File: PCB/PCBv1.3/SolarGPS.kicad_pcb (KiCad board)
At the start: 2 copper layers, 75 x 27 mm, 58 parts, among them J1 Conn_01x10_Female, J2 Solar1+, J3 GND, J4 Conn_02x03_Odd_Even, J5 Solar2+, J6 GND, J7 Screw_Terminal_01x01, J8 Conn_01x04_Male, U1 STM32L011G3Ux, U2 MAX-M10Q, U5 BQ25505, U6 LIS3DH, U7 TPS63802, Y1 32.768

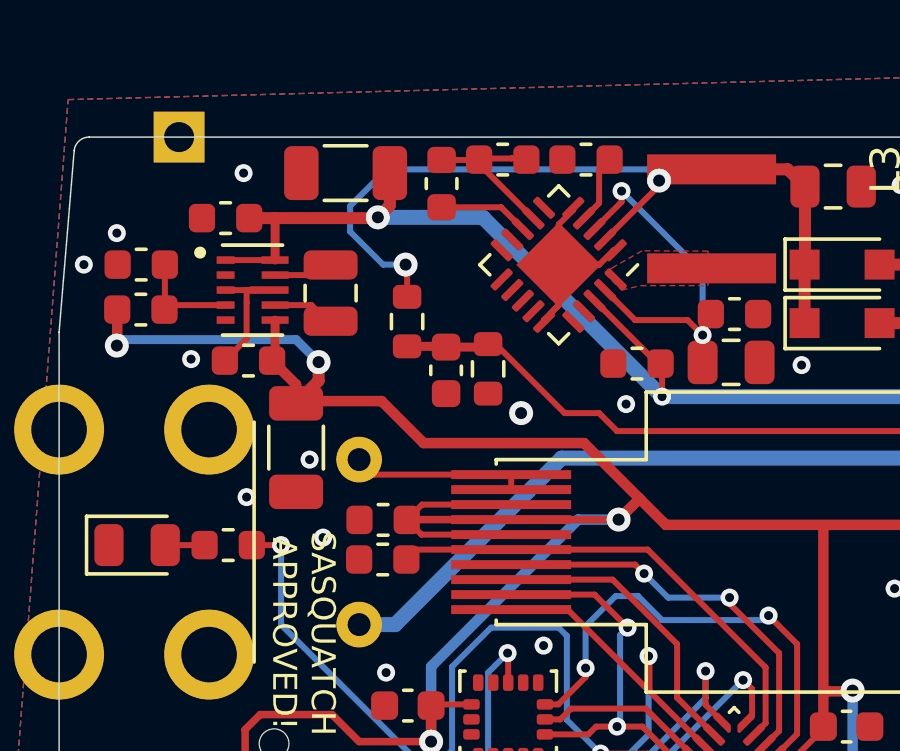
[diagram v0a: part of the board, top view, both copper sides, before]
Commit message: Move symbols to lib
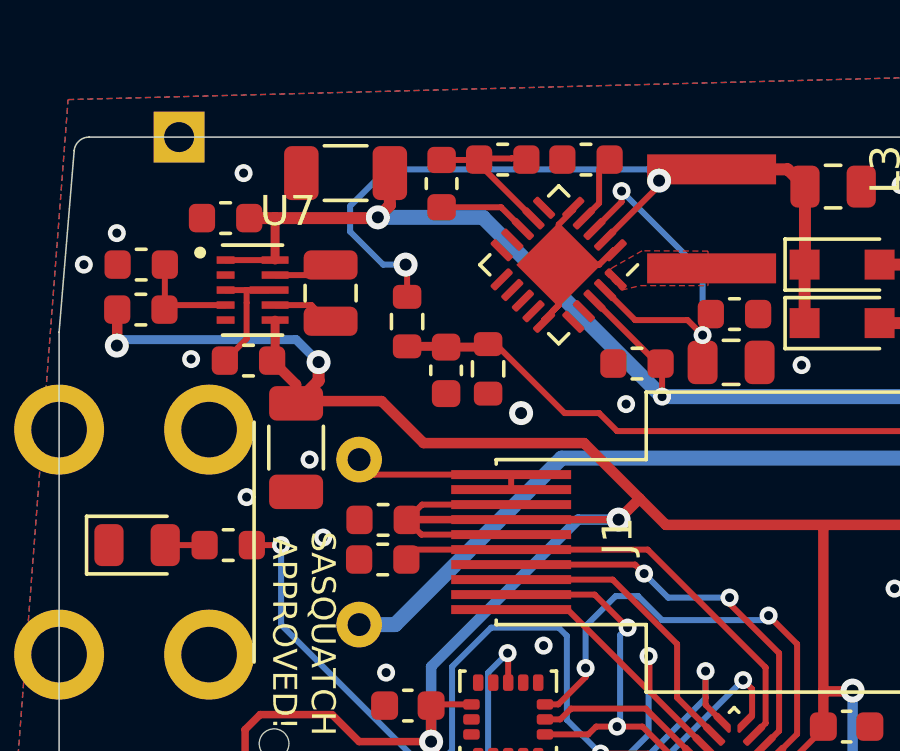
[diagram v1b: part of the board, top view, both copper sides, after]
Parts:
- C14: footprint Veridian-Library-KiCad:SCCT20E106SRB -> Heliograph:SCCT20E106SRB
- J1: footprint Margo_Lib:LS013B7DH03 -> Heliograph:LS013B7DH03
- L3: footprint Margo_Lib:744031220 -> Heliograph:744031220
- U7: footprint Margo_Lib:VREG_TPS63802DLAR -> Heliograph:VREG_TPS63802DLAR

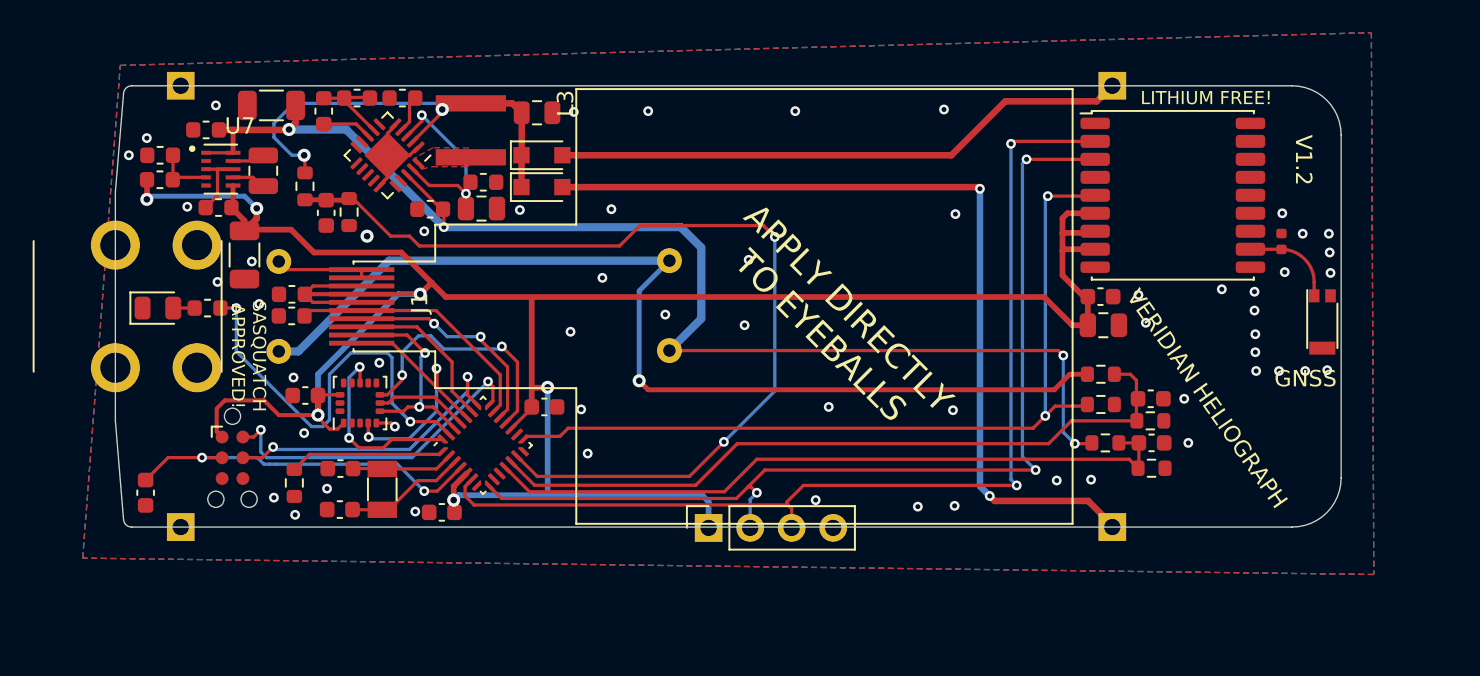
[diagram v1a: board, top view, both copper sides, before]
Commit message: Drop MPPT buck for diode cost
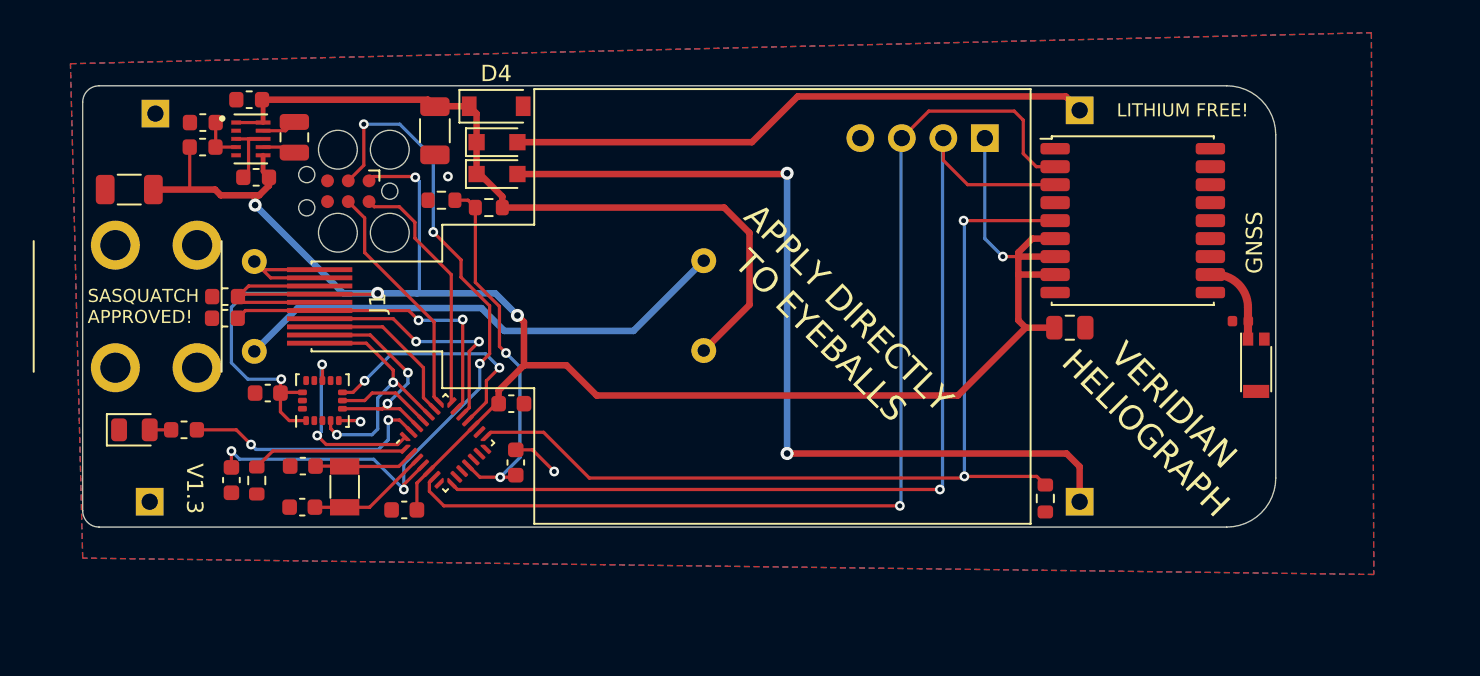
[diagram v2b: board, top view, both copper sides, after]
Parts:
- removed C15, C16, C19, C28, C6: 10nF, Capacitor_SMD:C_0603_1608Metric
- removed C2, C3: 4.7uF, Capacitor_SMD:C_0805_2012Metric
- removed C21: 1uF, Capacitor_SMD:C_0603_1608Metric
- removed L3: 22uH, Heliograph:744031220
- removed R14, R15, R2, R6: 1M, Resistor_SMD:R_0603_1608Metric
- removed ROV3: 4.30M, Resistor_SMD:R_0603_1608Metric
- removed ROV4: 8.66M, Resistor_SMD:R_0603_1608Metric
- removed U5: BQ25505, Package_DFN_QFN:QFN-20-1EP_3.5x3.5mm_P0.5mm_EP2x2mm
- added D4: 6V, Diode_SMD:D_SOD-123, F.Cu at (72.3, 51.2)
- J4: footprint Connector:Tag-Connect_TC2030-IDC-NL_2x03_P1.27mm_Vertical -> Connector:Tag-Connect_TC2030-IDC-FP_2x03_P1.27mm_Vertical
- J8: moved to B.Cu
- moved R13 46.4 mm to (69.0, 57.0), turned to 0 degrees
- moved R12 40.4 mm to (71.8, 57.5), turned to 0 degrees
- moved C23 38.9 mm to (73.5, 73.0), turned to -90 degrees
- moved J8 29.2 mm to (102.2, 53.2)
- moved J4 17.8 mm to (63.2, 56.5), turned to 180 degrees
- moved C12 10.1 mm to (68.5, 52.8), turned to 90 degrees
- moved C7 8.11 mm to (49.9, 56.4), turned to 0 degrees
- moved D2 7.59 mm to (50.2, 71.0)
- moved R3 7.59 mm to (53.2, 71.0)
- moved R7 6.68 mm to (105.9, 75.2), turned to 90 degrees
- moved C1 5.49 mm to (117.8, 64.4), turned to 0 degrees
- moved C18 5.31 mm to (56.1, 74.1)
- moved AE1 4.84 mm to (118.8, 67.1)
- moved C20 4.09 mm to (55.7, 64.2)
- moved C9 4.09 mm to (55.7, 62.9)
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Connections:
- D1 pad 1: SOLAR+ -> VBAT
- D3 pad 1: SOLAR+ -> VBAT
- U1 pad 12: VBATMID_SENSE -> unconnected-(U1-Pad12)
- U1 pad 13: SOLAR_SENSE1 -> unconnected-(U1-Pad13)
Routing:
- net SOLAR_SENSE1: track 58.7 -> 0.00 mm, vias 2 -> 0
- net VBATMID_SENSE: track 44.5 -> 0.00 mm
- net VBAT: track 79.5 -> 47.2 mm, vias 4 -> 0
- net VBATMID: track 62.4 -> 31.0 mm, vias 1 -> 0
- net SOLAR+: track 27.6 -> 0.00 mm, vias 2 -> 0
- net RESET: track 22.5 -> 47.4 mm, vias 2 -> 5
- net VBAT_SENSE: track 43.2 -> 22.8 mm, vias 0 -> 2
- net VSTOR: track 13.2 -> 0.00 mm, vias 2 -> 0
- net LED: track 25.8 -> 15.4 mm
- net VDD: track 156.3 -> 150.4 mm
- net Net-(ROV3-Pad1): track 5.22 -> 0.00 mm
- net GPS_EXINT: track 52.0 -> 57.0 mm
- net /SWDIO: track 20.3 -> 15.3 mm, vias 2 -> 0
- net /SWDCLK: track 18.4 -> 14.6 mm, vias 2 -> 0
- net DISP_EN: track 16.1 -> 19.9 mm, vias 0 -> 2
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- removed copper zone on F.Cu, net Net-(L3-Pad2)
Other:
- board size 75 x 27 mm -> 73 x 27 mm
- board text added: "V1.3"
- board text added: "VDD MOSI MISO GND"
- board text removed: "V1.2"

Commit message: Change LCD
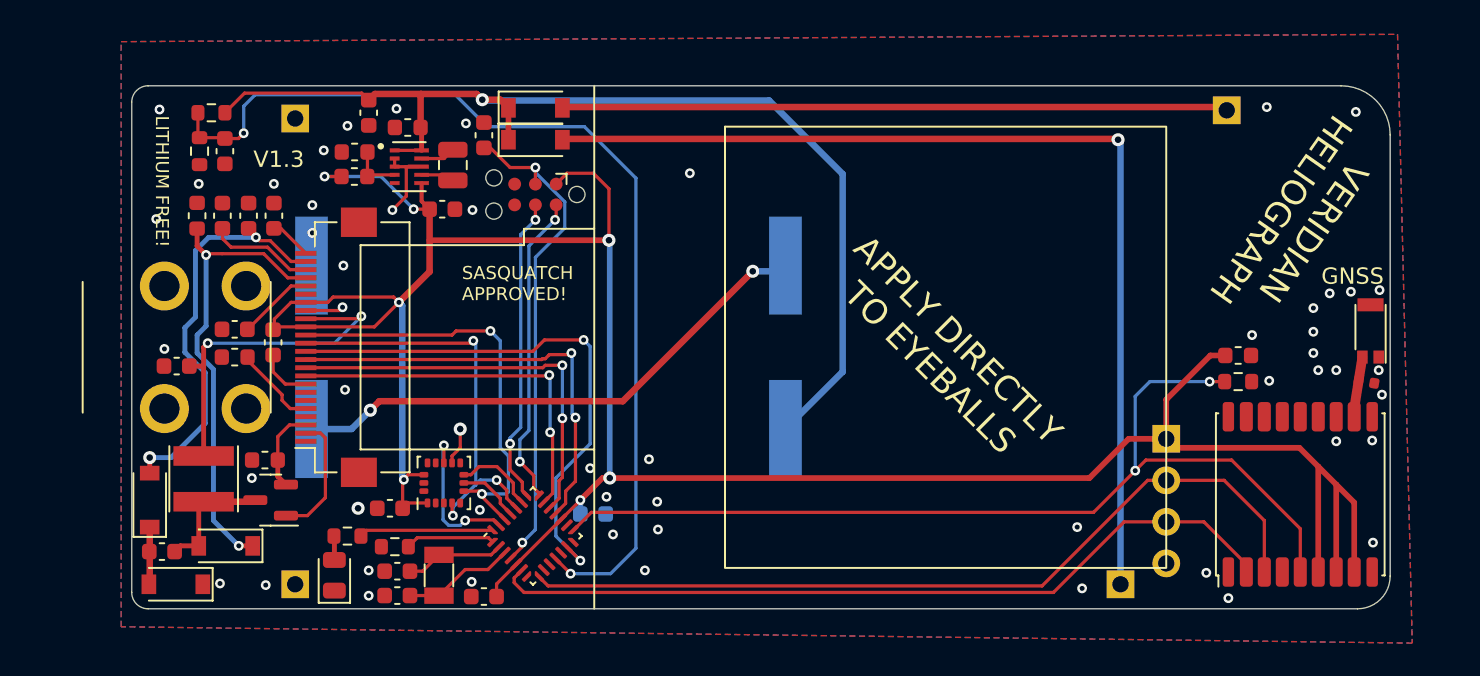
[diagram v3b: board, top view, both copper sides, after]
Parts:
- removed C23: 10nF, Capacitor_SMD:C_0603_1608Metric
- added C15: 1uF, Capacitor_SMD:C_0603_1608Metric, F.Cu at (58.6, 65.7)
- added C16: 1uF, Capacitor_SMD:C_0603_1608Metric, F.Cu at (52.8, 67.2)
- added C2: 1uF, Capacitor_SMD:C_0603_1608Metric, F.Cu at (58.7, 58.0)
- added C21: 1uF, Capacitor_SMD:C_0603_1608Metric, F.Cu at (57.1, 58.0)
- added C22: 1uF, Capacitor_SMD:C_0603_1608Metric, F.Cu at (51.9, 78.5)
- added C3: 1uF, Capacitor_SMD:C_0603_1608Metric, F.Cu at (55.5, 58.0)
- added C6: 1uF, Capacitor_SMD:C_0603_1608Metric, F.Cu at (56.3, 64.9)
- added D5: MBR0530, Diode_SMD:D_SOD-123, F.Cu at (51.1, 75.3)
- added D6: MBR0530, Diode_SMD:D_SOD-123, F.Cu at (52.7, 80.5)
- added L1: 47uH, Inductor_SMD:L_Taiyo-Yuden_NR-40xx, F.Cu at (54.4, 74.0)
- added Q1: Q_NMOS_GSD, Package_TO_SOT_SMD:SOT-23, F.Cu at (58.5, 75.3)
- added R2: 149, Resistor_SMD:R_0603_1608Metric, F.Cu at (63.2, 77.5)
- added REF**: ER-EPD0154-2R, Heliograph:ER-EPD0154-2R, F.Cu at (64.0, 66.0)
- C11: moved to B.Cu
- C12, C7: value 47uF -> 22uF; footprint Capacitor_SMD:C_1206_3216Metric -> Capacitor_SMD:C_0603_1608Metric
- C13: value 4.7uF -> 1uF; footprint Capacitor_SMD:C_0805_2012Metric -> Capacitor_SMD:C_0603_1608Metric
- C14: footprint Heliograph:SCCT20E106SRB -> Heliograph:SCCT20E106SRB_SMD
- C17: footprint Veridian-Library-KiCad:SCCT20E106SRB -> Heliograph:SCCT20E106SRB_SMD
- C18: value 10nF -> 1uF
- C5: value 10nF -> 22uF
- D1, D3: value Schottky -> MBR0530; footprint Diode_SMD:D_SOD-323_HandSoldering -> Diode_SMD:D_SOD-123
- D4: value 6V -> MBR0530
- J1: value Conn_01x10_Female -> Conn_01x24_Female; footprint Heliograph:LS013B7DH03 -> Connector_FFC-FPC:Hirose_FH12-24S-0.5SH_1x24-1MP_P0.50mm_Horizontal
- J4: footprint Connector:Tag-Connect_TC2030-IDC-FP_2x03_P1.27mm_Vertical -> Connector:Tag-Connect_TC2030-IDC-NL_2x03_P1.27mm_Vertical
- R3: value 390 -> 2.2
- U1: value STM32L011G3Ux -> STM32L011G4Ux
- moved C5 61.1 mm to (117.7, 66.5)
- moved C13 52.8 mm to (55.7, 54.0), turned to 90 degrees
- moved D4 31.6 mm to (55.8, 78.2), turned to 180 degrees
- moved C18 26.2 mm to (71.5, 53.0), turned to -90 degrees
- moved J8 21.5 mm to (113.3, 71.6), turned to 180 degrees
- moved U2 19.6 mm to (121.5, 75.0), turned to 90 degrees
- moved C7 19.2 mm to (69.0, 57.5), turned to 180 degrees
- moved R12 17.9 mm to (54.9, 51.6)
- moved D2 15.1 mm to (62.4, 80.0), turned to 90 degrees
- moved R13 15.1 mm to (54.1, 54.0), turned to 90 degrees
- moved R7 13.8 mm to (117.7, 68.1), turned to 180 degrees
- moved J4 11.5 mm to (74.7, 56.6)
- moved C26 10.3 mm to (65.8, 75.8)
- moved J6 10.2 mm to (60.0, 80.5)
- moved L2 9.85 mm to (69.7, 54.9)
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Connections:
- net VBATMID renamed Net-(C14-Pad2)
- C13 pad 1: VDD -> GND
- C13 pad 2: GND -> VBAT_SENSE
- C20 pad 1: GND -> /VGH
- C20 pad 2: DISP_EN -> GND
- C5 pad 1: GND -> VDD
- C5 pad 2: VDD -> GND
- C9 pad 1: GND -> /VSH2
- C9 pad 2: VDD -> GND
- D4 pad 1: VBAT -> /VGH
- D4 pad 2: GND -> Net-(C22-Pad1)
- J1 pad 1: SPI_CLK -> unconnected-(J1-Pad1)
- J1 pad 10: GND -> DISP_RES#
- J1 pad 2: SPI_MOSI -> /GDR
- J1 pad 3: DISP_CS -> /RESE
- J1 pad 4: EXTCOMIN -> unconnected-(J1-Pad4)
- J1 pad 5: DISP_EN -> /VSH2
- J1 pad 6: VDD -> unconnected-(J1-Pad6)
- J1 pad 7: VDD -> unconnected-(J1-Pad7)
- J1 pad 8: VDD -> GND
- J1 pad 9: GND -> DISP_BUSY
- R3 pad 1: LED -> GND
- R3 pad 2: Net-(D2-Pad2) -> /RESE
- U1 pad 13: unconnected-(U1-Pad13) -> DISP_CS
- U1 pad 18: LIS_CS -> DISP_DC
- U1 pad 19: EXTCOMIN -> DISP_RES#
- U1 pad 20: DISP_EN -> DISP_BUSY
- U1 pad 23: DISP_CS -> LIS_CS
- U1 pad 27: LED -> LIS_INT
- U1 pad 28: LIS_INT -> LED
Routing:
- net VBAT_SENSE: track 22.8 -> 61.1 mm
- net /VGH: track 0.00 -> 28.5 mm, vias 0 -> 2
- net DISP_DC: track 0.00 -> 26.9 mm, vias 0 -> 2
- net /VGL: track 0.00 -> 25.0 mm, vias 0 -> 2
- net DISP_RES#: track 0.00 -> 24.8 mm, vias 0 -> 2
- net DISP_CS: track 10.2 -> 33.6 mm, vias 0 -> 2
- net DISP_BUSY: track 0.00 -> 23.0 mm, vias 0 -> 2
- net /VCI: track 0.00 -> 21.8 mm, vias 0 -> 2
- net DISP_EN: track 19.9 -> 0.00 mm, vias 2 -> 0
- net VBAT: track 47.2 -> 66.6 mm, vias 0 -> 1
- net RESET: track 47.4 -> 30.3 mm, vias 5 -> 2
- net GPS_UART_MISO: track 65.4 -> 49.4 mm, vias 1 -> 0
- net EXTCOMIN: track 15.2 -> 0.00 mm, vias 2 -> 0
- net VDD: track 150.4 -> 164.7 mm, vias 6 -> 7
- net SPI_MOSI: track 14.5 -> 26.7 mm
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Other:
- board size 73 x 27 mm -> 77 x 32 mm
